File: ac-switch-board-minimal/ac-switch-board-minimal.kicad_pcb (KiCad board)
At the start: 2 copper layers, 73 parts, among them CON1 AVR-ISP-10, J1 AC_IN, J10 BACKUP_VOUT, J11 BACKUP_VIN, J12 CH0_AC, J13 CH1_AC, J2 DIGITS, J3 SEGMENTS, J4 DISP0_EXTRAS, J5 DISP1_EXTRAS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

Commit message: board progress
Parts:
- added J14: UART, Pin_Headers:Pin_Header_Straight_1x02_Pitch2.54mm, F.Cu at (148.0, 94.0)
- added J15: Conn_01x01, Pin_Headers:Pin_Header_Straight_1x01_Pitch2.54mm, F.Cu at (167.0, 96.5)
- added J16: SEGMENTS1, Pin_Headers:Pin_Header_Straight_1x08_Pitch2.54mm, F.Cu at (127.0, 95.9)
- CON1: value AVR-ISP-10 -> AVR-ISP-6; footprint Connectors:IDC_Header_Straight_10pins -> Connectors:IDC_Header_Straight_6pins
- J3: value SEGMENTS -> SEGMENTS0
- R11, R9: footprint Resistors_THT:R_Axial_DIN0207_L6.3mm_D2.5mm_P10.16mm_Horizontal -> Resistors_THT:R_Axial_DIN0207_L6.3mm_D2.5mm_P5.08mm_Vertical
- moved LS1 161.2 mm to (91.8, 86.0), turned to 180 degrees
- moved Q2 154.8 mm to (91.8, 92.4), turned to 270 degrees
- moved Q1 154.3 mm to (91.8, 75.9), turned to 270 degrees
- moved LS2 148.2 mm to (91.8, 102.6), turned to 180 degrees
- moved R9 146.9 mm to (97.2, 80.6), turned to 270 degrees
- moved R11 141.3 mm to (97.2, 97.8), turned to 270 degrees
- moved R10 140.5 mm to (97.5, 75.9), turned to 90 degrees
- moved R12 132.4 mm to (97.5, 92.4), turned to 90 degrees
- moved J11 106.5 mm to (120.0, 48.3), turned to 270 degrees
- moved J3 84.4 mm to (127.0, 99.7), turned to 270 degrees
- moved R2 77.3 mm to (118.1, 102.9), turned to 0 degrees
- moved C15 71.5 mm to (160.5, 71.1)
- moved C17 71.5 mm to (158.0, 67.3)
- moved F1 71.5 mm to (179.1, 35.6)
- moved J12 71.5 mm to (158.8, 38.7)
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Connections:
- CON1 pad 3: Net-(CON1-Pad3) -> /SCK
- CON1 pad 4: Net-(CON1-Pad10) -> /MISO
- CON1 pad 6: Net-(CON1-Pad10) -> GND
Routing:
- net +15V: track 11.0 -> 24.2 mm
- net GND: track 72.0 -> 84.0 mm
- net Net-(R3-Pad2): track 16.1 -> 7.05 mm
- net Net-(J14-Pad2): track 0.00 -> 7.62 mm
- net Net-(J14-Pad1): track 0.00 -> 7.62 mm
- net /AC_IN_NEUT: track 16.0 -> 11.6 mm
- net Net-(C11-Pad1): track 3.45 -> 2.18 mm
- net /AC_IN_HOT: track 16.1 -> 16.7 mm

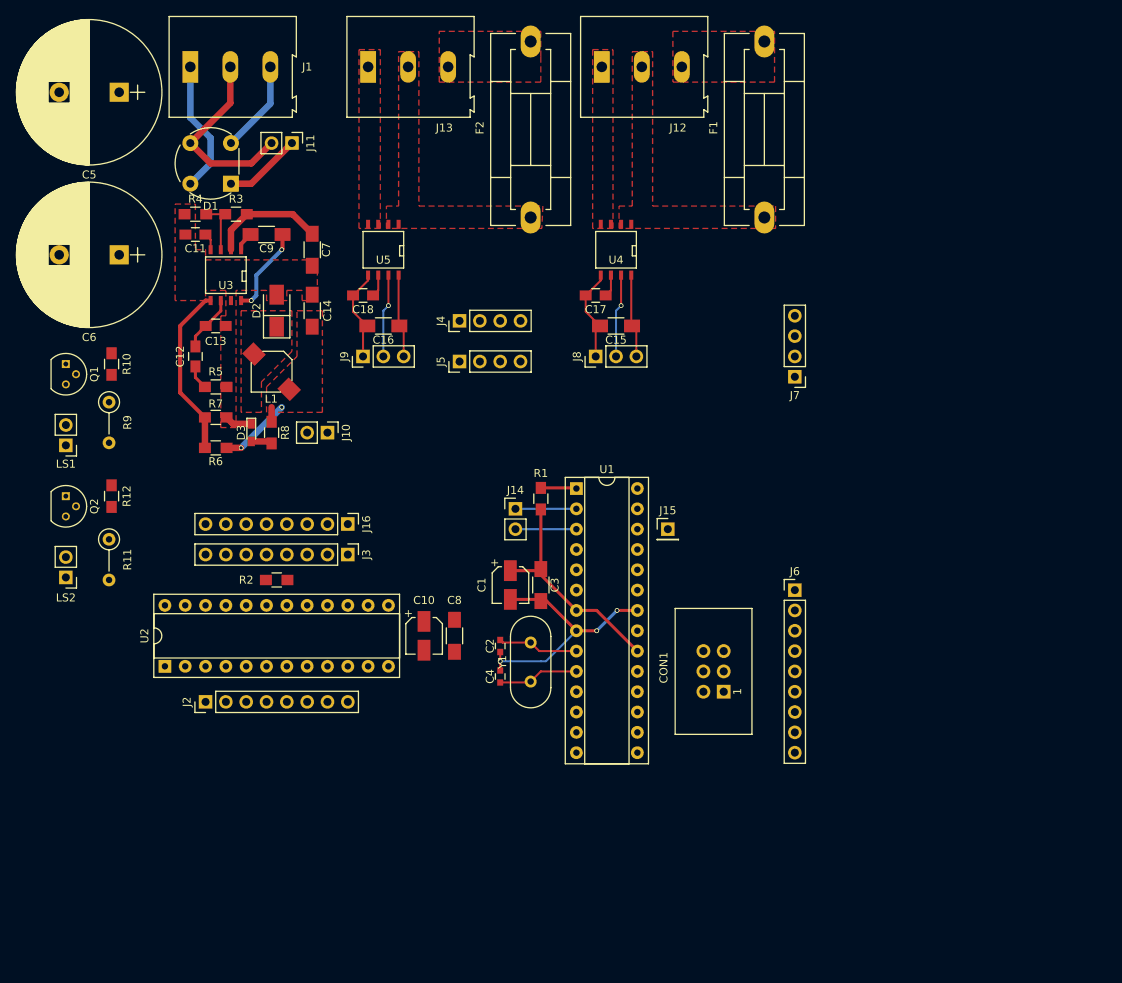
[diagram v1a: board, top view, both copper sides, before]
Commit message: board completely routed
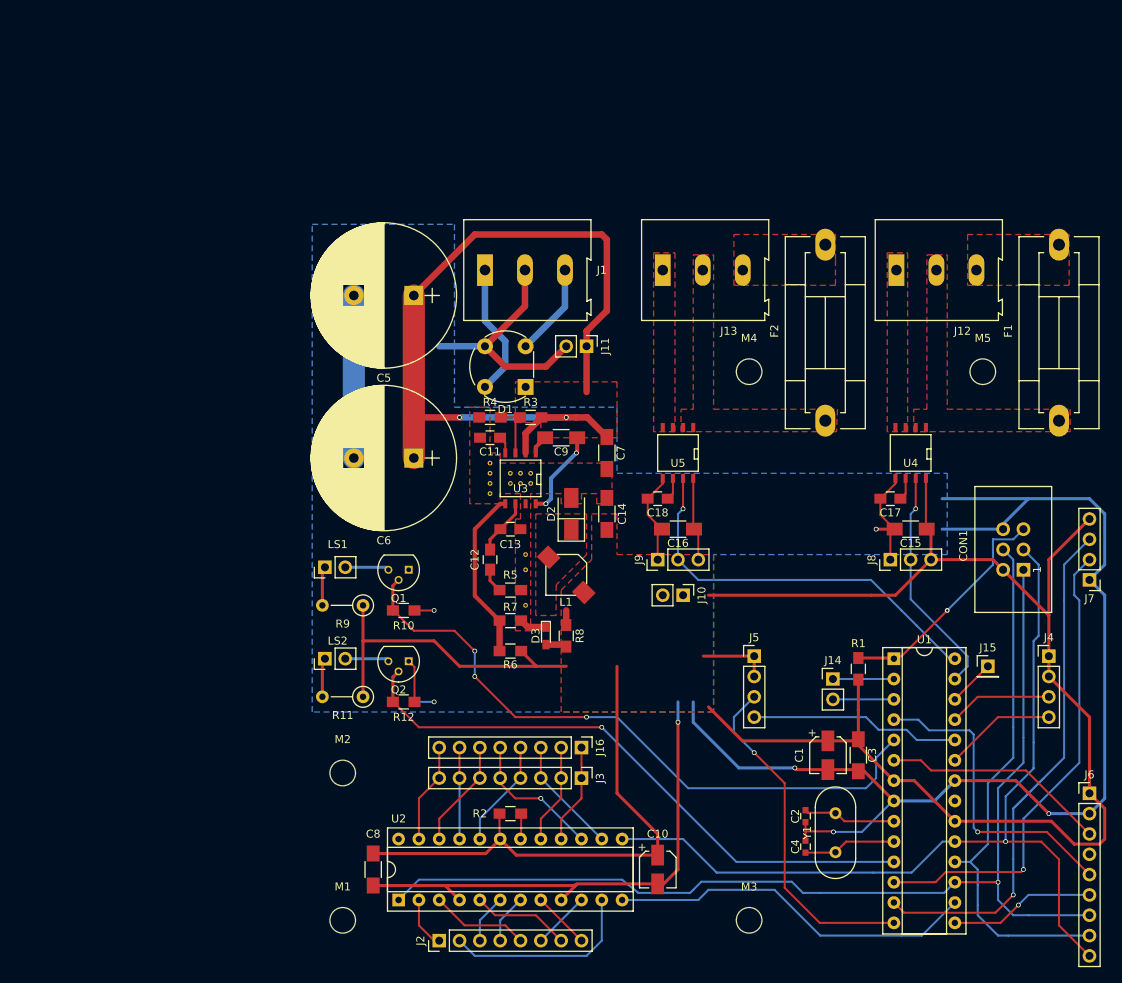
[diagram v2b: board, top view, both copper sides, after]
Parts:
- added M1: MountingHole_3.2mm_M3, Mounting_Holes:MountingHole_3.2mm_M3, F.Cu at (126.4, 145.4)
- added M2: MountingHole_3.2mm_M3, Mounting_Holes:MountingHole_3.2mm_M3, F.Cu at (126.4, 127.0)
- added M3: MountingHole_3.2mm_M3, Mounting_Holes:MountingHole_3.2mm_M3, F.Cu at (177.2, 145.4)
- added M4: MountingHole_3.2mm_M3, Mounting_Holes:MountingHole_3.2mm_M3, F.Cu at (177.2, 76.8)
- added M5: MountingHole_3.2mm_M3, Mounting_Holes:MountingHole_3.2mm_M3, F.Cu at (206.4, 76.8)
- added REF**: Via_0.6mm_Thermal, footprints:Via_0.6mm_Tented, F.Cu at (149.9, 89.5)
- added REF**: Via_0.6mm_Thermal, footprints:Via_0.6mm_Tented, F.Cu at (144.8, 89.5)
- added REF**: Via_0.6mm_Tented, footprints:Via_0.6mm_Tented, F.Cu at (149.2, 106.0)
- added REF**: Via_0.6mm_Thermal, footprints:Via_0.6mm_Thermal, F.Cu at (144.8, 90.8)
- added REF**: Via_0.6mm_Thermal, footprints:Via_0.6mm_Thermal, F.Cu at (144.8, 92.1)
- added REF**: Via_0.6mm_Thermal, footprints:Via_0.6mm_Thermal, F.Cu at (144.8, 88.3)
- added REF**: Via_0.6mm_Thermal, footprints:Via_0.6mm_Tented, F.Cu at (147.3, 90.8)
- added REF**: Via_0.6mm_Thermal, footprints:Via_0.6mm_Tented, F.Cu at (149.9, 90.8)
- added REF**: Via_0.6mm_Thermal, footprints:Via_0.6mm_Tented, F.Cu at (148.6, 90.8)
- added REF**: Via_0.6mm_Thermal, footprints:Via_0.6mm_Tented, F.Cu at (148.6, 89.5)
- added REF**: Via_0.6mm_Tented, footprints:Via_0.6mm_Tented, F.Cu at (147.3, 89.5)
- added REF**: Via_0.6mm_Thermal, footprints:Via_0.6mm_Thermal, F.Cu at (149.2, 99.7)
- added REF**: Via_0.6mm_Tented, footprints:Via_0.6mm_Tented, F.Cu at (149.2, 101.6)
- added REF**: Via_0.6mm_Thermal, footprints:Via_0.6mm_Tented, F.Cu at (147.3, 89.5)
- moved J4 84.7 mm to (214.6, 112.4), turned to 0 degrees
- moved J5 52.1 mm to (177.8, 112.4), turned to 0 degrees
- moved Q1 50.0 mm to (134.6, 101.6), turned to 180 degrees
- moved J10 48.9 mm to (168.9, 104.8)
- moved R10 47.8 mm to (134.0, 106.7), turned to 0 degrees
- moved Q2 47.6 mm to (134.6, 113.0), turned to 180 degrees
- moved C1 45.0 mm to (187.0, 124.8)
- moved C3 45.0 mm to (190.8, 124.8)
- moved R1 45.0 mm to (190.8, 114.0)
- moved U1 45.0 mm to (195.3, 112.7)
- moved J14 45.0 mm to (187.6, 115.3)
- moved ? 44.7 mm to (142.2, 97.8)
- moved ? 44.7 mm to (149.9, 90.8)
- moved ? 44.7 mm to (146.1, 90.8)
- moved F1 44.7 mm to (215.9, 61.0)
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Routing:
- net +5V: track 60.7 -> 298.8 mm, vias 2 -> 0
- net GND: track 84.0 -> 302.2 mm, vias 3 -> 6
- net /MOSI: track 0.00 -> 133.2 mm, vias 0 -> 1
- net /SCK: track 0.00 -> 112.2 mm, vias 0 -> 1
- net /AUD1: track 0.00 -> 82.3 mm, vias 0 -> 3
- net +15V: track 24.2 -> 101.5 mm, vias 0 -> 2
- net /AUD2: track 0.00 -> 75.0 mm, vias 0 -> 1
- net /CH1_EN: track 0.00 -> 70.2 mm, vias 0 -> 1
- net /MISO: track 0.00 -> 65.8 mm
- net /CH0_EN: track 0.00 -> 59.5 mm, vias 0 -> 1
- net /DISPLAY_SS: track 0.00 -> 46.2 mm
- net /DISP_EXTRA_1: track 0.00 -> 43.0 mm, vias 0 -> 1
- net /CH1_VIOUT: track 10.4 -> 50.3 mm
- net /IRQ: track 0.00 -> 39.3 mm, vias 0 -> 1
- net /BLUEFRUIT_RST: track 0.00 -> 28.3 mm
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- added copper zone on F.Cu, net +15V
- added copper zone on B.Cu, net GND
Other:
- rule trace_min: 0.1524 -> 0.1778

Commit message: Added silkscreen info
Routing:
- net +5V: track 298.8 -> 290.2 mm, vias 0 -> 1
- net /CH1_EN: track 70.2 -> 64.8 mm
- net (no net): track 2.54 -> 0.00 mm, vias 1 -> 0
- net GND: track 302.2 -> 304.5 mm, vias 6 -> 7
- net /CH0_EN: track 59.5 -> 58.2 mm
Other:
- board text added: "5V DC"
- board text added: "AVR"
- board text added: "BLE"
- board text added: "Bluetooth Controlled AC Switch"
- board text added: "ECE 342 - W18"
- board text added: "Group 5 Alive"
- board text added: "Layout: Spencer Moss"
- board text added: "MAX7221"
- board text added: "Relays"
- board text added: "Sound System"
- board text added: "Team: Spencer Moss, Jacob Ficker, Jesus Narvaez"
- board text added: "^^^DANGER!^^^ HIGH VOLTAGE"
- board text added: "rev 1"

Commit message: More small board tweaks
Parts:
- added D4: LED, Pin_Headers:Pin_Header_Straight_1x02_Pitch2.54mm, F.Cu at (69.8, 114.9)
- added R13: 220, Resistors_SMD:R_0805_HandSoldering, F.Cu at (71.1, 110.5)
- moved ? 94.4 mm to (56.5, 75.6)
- moved ? 94.4 mm to (56.5, 76.8)
- moved ? 94.4 mm to (52.7, 75.6)
- moved ? 94.4 mm to (52.7, 76.8)
- moved C10 94.4 mm to (72.4, 125.1)
- moved C17 94.4 mm to (101.5, 78.7)
- moved C18 94.4 mm to (72.4, 78.7)
- moved C2 94.4 mm to (90.9, 118.4)
- moved C4 94.4 mm to (90.9, 122.2)
- moved C8 94.4 mm to (36.8, 125.1)
- moved CON1 94.4 mm to (118.1, 87.6)
- moved J1 94.4 mm to (50.8, 50.2)
- moved J12 94.4 mm to (102.2, 50.2)
- moved J14 94.4 mm to (94.3, 101.3)
- moved J5 94.4 mm to (84.5, 98.4)
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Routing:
- net GND: track 304.5 -> 295.4 mm, vias 7 -> 9
- net Net-(D4-Pad2): track 0.00 -> 4.48 mm
- net +5V: track 290.2 -> 286.7 mm
- net /SCK: track 112.2 -> 111.6 mm
- net /DISPLAY_SS: track 46.2 -> 45.7 mm
- net /CH0_VIOUT: vias 1 -> 0
- net /CH1_VIOUT: vias 1 -> 0
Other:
- board outline added: 100.3 x 94.6 mm
- rule trace_min: 0.1778 -> 0.15
- rule via_min_size: 0.4 -> 0.3

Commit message: Board work
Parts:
- J14: footprint Pin_Headers:Pin_Header_Straight_1x02_Pitch2.54mm -> Pin_Headers:Pin_Header_Straight_1x03_Pitch2.54mm
- moved J14 4.51 mm to (90.8, 98.4)
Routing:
- net GND: track 295.4 -> 312.4 mm
- net Net-(J14-Pad2): track 7.62 -> 19.9 mm
- net Net-(J14-Pad1): track 7.62 -> 19.9 mm
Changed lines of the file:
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@@
 (kicad_pcb (version 4) (host pcbnew 4.0.7)
   (general
-    (links 182)
+    (links 183)
     (no_connects 0)
     (area 28.499999 43.104999 128.980001 137.870001)
     (thickness 1.6)
     (drawings 54)
-    (tracks 442)
+    (tracks 450)
     (zones 0)
     (modules 97)
@@
     )
   )
-  (module Pin_Headers:Pin_Header_Straight_1x02_Pitch2.54mm (layer F.Cu)
-    (at 94.2975 101.2825)
-    (descr "Through hole straight pin header, 1x02, 2.54mm pitch, single row")
-    (tags "Through hole pin header THT 1x02 2.54mm single row")
-    (fp_text reference J14 (at 0 -2.33) (layer F.SilkS)
-      (effects (font (size 1 1) (thickness 0.15)))
-    )
-    (fp_text value UART (at 0 4.87) (layer F.Fab)
-      (effects (font (size 1 1) (thickness 0.15)))
-    )
-    (fp_line (start -0.635 -1.27) (end 1.27 -1.27) (layer F.Fab) (width 0.1))
-    (fp_line (start 1.27 -1.27) (end 1.27 3.81) (layer F.Fab) (width 0.1))
-    (fp_line (start 1.27 3.81) (end -1.27 3.81) (layer F.Fab) (width 0.1))
-    (fp_line (start -1.27 3.81) (end -1.27 -0.635) (layer F.Fab) (width 0.1))
-    (fp_line (start -1.27 -0.635) (end -0.635 -1.27) (layer F.Fab) (width 0.1))
-    (fp_line (start -1.33 3.87) (end 1.33 3.87) (layer F.SilkS) (width 0.12))
-    (fp_line (start -1.33 1.27) (end -1.33 3.87) (layer F.SilkS) (width 0.12))
-    (fp_line (start 1.33 1.27) (end 1.33 3.87) (layer F.SilkS) (width 0.12))
-    (fp_line (start -1.33 1.27) (end 1.33 1.27) (layer F.SilkS) (width 0.12))
-    (fp_line (start -1.33 0) (end -1.33 -1.33) (layer F.SilkS) (width 0.12))
-    (fp_line (start -1.33 -1.33) (end 0 -1.33) (layer F.SilkS) (width 0.12))
-    (fp_line (start -1.8 -1.8) (end -1.8 4.35) (layer F.CrtYd) (width 0.05))
-    (fp_line (start -1.8 4.35) (end 1.8 4.35) (layer F.CrtYd) (width 0.05))
-    (fp_line (start 1.8 4.35) (end 1.8 -1.8) (layer F.CrtYd) (width 0.05))
-    (fp_line (start 1.8 -1.8) (end -1.8 -1.8) (layer F.CrtYd) (width 0.05))
-    (fp_text user %R (at 0 1.27 90) (layer F.Fab)
-      (effects (font (size 1 1) (thickness 0.15)))
-    )
-    (pad 1 thru_hole rect (at 0 0) (size 1.7 1.7) (drill 1) (layers *.Cu *.Mask)
-      (net 67 "Net-(J14-Pad1)"))
-    (pad 2 thru_hole oval (at 0 2.54) (size 1.7 1.7) (drill 1) (layers *.Cu *.Mask)
-      (net 68 "Net-(J14-Pad2)"))
-    (model ${KISYS3DMOD}/Pin_Headers.3dshapes/Pin_Header_Straight_1x02_Pitch2.54mm.wrl
-      (at (xyz 0 0 0))
-      (scale (xyz 1 1 1))
-      (rotate (xyz 0 0 0))
-    )
-  )
   (module Pin_Headers:Pin_Header_Straight_1x01_Pitch2.54mm (layer F.Cu)
     (at 113.665 99.695)
@@
     )
   )
+  (module Pin_Headers:Pin_Header_Straight_1x03_Pitch2.54mm (layer F.Cu)
+    (at 90.805 98.425)
+    (descr "Through hole straight pin header, 1x03, 2.54mm pitch, single row")
+    (tags "Through hole pin header THT 1x03 2.54mm single row")
+    (fp_text reference J14 (at 0 -2.33) (layer F.SilkS)
+      (effects (font (size 1 1) (thickness 0.15)))
+    )
+    (fp_text value UART (at 0 7.41) (layer F.Fab)
+      (effects (font (size 1 1) (thickness 0.15)))
+    )
+    (fp_line (start -0.635 -1.27) (end 1.27 -1.27) (layer F.Fab) (width 0.1))
+    (fp_line (start 1.27 -1.27) (end 1.27 6.35) (layer F.Fab) (width 0.1))
+    (fp_line (start 1.27 6.35) (end -1.27 6.35) (layer F.Fab) (width 0.1))
+    (fp_line (start -1.27 6.35) (end -1.27 -0.635) (layer F.Fab) (width 0.1))
+    (fp_line (start -1.27 -0.635) (end -0.635 -1.27) (layer F.Fab) (width 0.1))
+    (fp_line (start -1.33 6.41) (end 1.33 6.41) (layer F.SilkS) (width 0.12))
+    (fp_line (start -1.33 1.27) (end -1.33 6.41) (layer F.SilkS) (width 0.12))
+    (fp_line (start 1.33 1.27) (end 1.33 6.41) (layer F.SilkS) (width 0.12))
+    (fp_line (start -1.33 1.27) (end 1.33 1.27) (layer F.SilkS) (width 0.12))
+    (fp_line (start -1.33 0) (end -1.33 -1.33) (layer F.SilkS) (width 0.12))
+    (fp_line (start -1.33 -1.33) (end 0 -1.33) (layer F.SilkS) (width 0.12))
+    (fp_line (start -1.8 -1.8) (end -1.8 6.85) (layer F.CrtYd) (width 0.05))
+    (fp_line (start -1.8 6.85) (end 1.8 6.85) (layer F.CrtYd) (width 0.05))
+    (fp_line (start 1.8 6.85) (end 1.8 -1.8) (layer F.CrtYd) (width 0.05))
+    (fp_line (start 1.8 -1.8) (end -1.8 -1.8) (layer F.CrtYd) (width 0.05))
+    (fp_text user %R (at 0 2.54 90) (layer F.Fab)
+      (effects (font (size 1 1) (thickness 0.15)))
+    )
+    (pad 1 thru_hole rect (at 0 0) (size 1.7 1.7) (drill 1) (layers *.Cu *.Mask)
+      (net 67 "Net-(J14-Pad1)"))
+    (pad 2 thru_hole oval (at 0 2.54) (size 1.7 1.7) (drill 1) (layers *.Cu *.Mask)
+      (net 68 "Net-(J14-Pad2)"))
+    (pad 3 thru_hole oval (at 0 5.08) (size 1.7 1.7) (drill 1) (layers *.Cu *.Mask)
+      (net 2 GND))
+    (model ${KISYS3DMOD}/Pin_Headers.3dshapes/Pin_Header_Straight_1x03_Pitch2.54mm.wrl
+      (at (xyz 0 0 0))
+      (scale (xyz 1 1 1))
+      (rotate (xyz 0 0 0))
+    )
+  )
   (gr_line (start 71.755 74.93) (end 71.755 73.66) (angle 90) (layer Edge.Cuts) (width 0.15))
   (gr_line (start 69.85 74.93) (end 71.755 74.93) (angle 90) (layer Edge.Cuts) (width 0.15))
@@
   (segment (start 97.2725 109.0075) (end 97.4725 108.8075) (width 0.381) (layer F.Cu) (net 1) (status 30))
   (segment (start 60.96 94.535) (end 60.96 92.71) (width 0.8128) (layer F.Cu) (net 1) (status 10))
+  (segment (start 78.74 95.25) (end 85.09 95.25) (width 0.254) (layer B.Cu) (net 2))
+  (segment (start 87.63 100.33) (end 90.805 103.505) (width 0.254) (layer B.Cu) (net 2))
+  (segment (start 87.63 97.79) (end 87.63 100.33) (width 0.254) (layer B.Cu) (net 2))
+  (segment (start 85.09 95.25) (end 87.63 97.79) (width 0.254) (layer B.Cu) (net 2))
   (segment (start 69.85 114.935) (end 69.85 116.205) (width 0.254) (layer F.Cu) (net 2))
   (segment (start 71.12 117.475) (end 74.93 117.475) (width 0.254) (layer F.Cu) (net 2))
@@
   (segment (start 52.705 79.375) (end 49.53 82.55) (width 0.508) (layer F.Cu) (net 66))
   (segment (start 52.625 93.98) (end 52.625 97.79) (width 0.8128) (layer F.Cu) (net 66) (status 30))
+  (segment (start 101.9175 101.2825) (end 93.6625 101.2825) (width 0.254) (layer B.Cu) (net 67))
+  (segment (start 93.6625 101.2825) (end 90.805 98.425) (width 0.254) (layer B.Cu) (net 67))
   (segment (start 94.2975 101.2825) (end 101.9175 101.2825) (width 0.254) (layer B.Cu) (net 67) (status 30))
+  (segment (start 101.9175 103.8225) (end 93.6625 103.8225) (width 0.254) (layer B.Cu) (net 68))
+  (segment (start 93.6625 103.8225) (end 90.805 100.965) (width 0.254) (layer B.Cu) (net 68))
   (segment (start 101.9175 103.8225) (end 94.2975 103.8225) (width 0.254) (layer B.Cu) (net 68) (status 30))
   (segment (start 113.665 99.695) (end 109.5375 103.8225) (width 0.254) (layer F.Cu) (net 69) (status 30))

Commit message: Board things, including errata list for next version
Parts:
- added J17: XTRA_GND, Pin_Headers:Pin_Header_Straight_1x03_Pitch2.54mm, F.Cu at (87.6, 83.8)
- turned R2 to 180 degrees
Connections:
- CON1 pad 1: /MOSI -> /MISO
- CON1 pad 4: /MISO -> /MOSI
- D2 pad 1: Net-(D2-Pad1) -> Net-(C9-Pad1)
- L1 pad 1: Net-(D2-Pad1) -> Net-(C9-Pad1)
- R2 pad 1: +5V -> Net-(R2-Pad1)
- R2 pad 2: Net-(R2-Pad2) -> +5V
- U2 pad 18: Net-(R2-Pad2) -> Net-(R2-Pad1)
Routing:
- net /MOSI: track 132.8 -> 136.7 mm, vias 1 -> 3
- net Net-(R2-Pad2): track 3.21 -> 0.00 mm
- net Net-(R2-Pad1): track 0.00 -> 3.21 mm
- net /MISO: track 66.1 -> 63.6 mm
- added copper zone on F.Cu, net Net-(C9-Pad1)
- removed copper zone on F.Cu, net Net-(D2-Pad1)
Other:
- outline, holes or cut-outs redrawn
